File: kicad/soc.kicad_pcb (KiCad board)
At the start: 2 copper layers, 104.1 x 63.5 mm, 18 parts, among them J1 Line Out, J2 PS/2 Keyboard, J3 PS/2 Mouse, J4 Line In, P1 LED MATRIX, P10 CODEC right, P2 ALTERA_DE1_GPIO, P3 Bluetooth, P4 CONN_01X09, P9 CODEC left, U2 DS3234

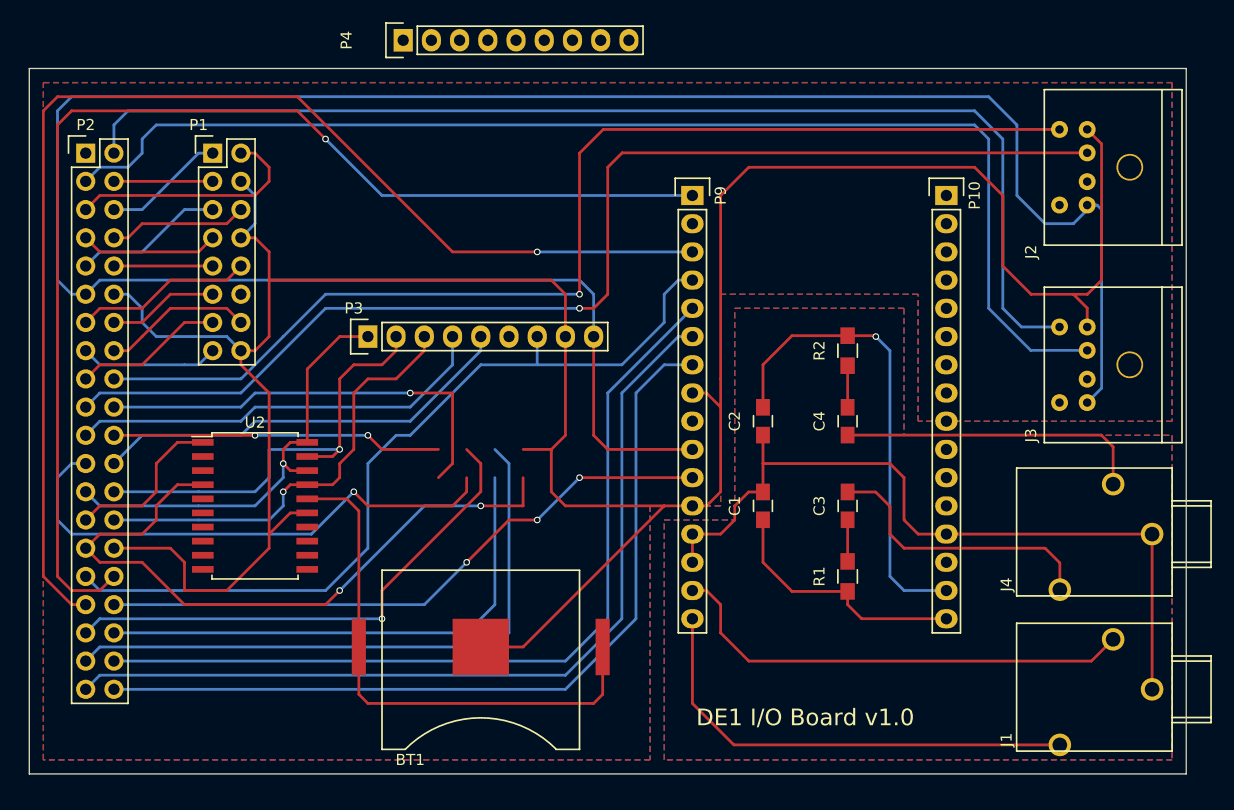
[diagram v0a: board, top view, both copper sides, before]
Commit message: new I/O board to test SSM2603 codec
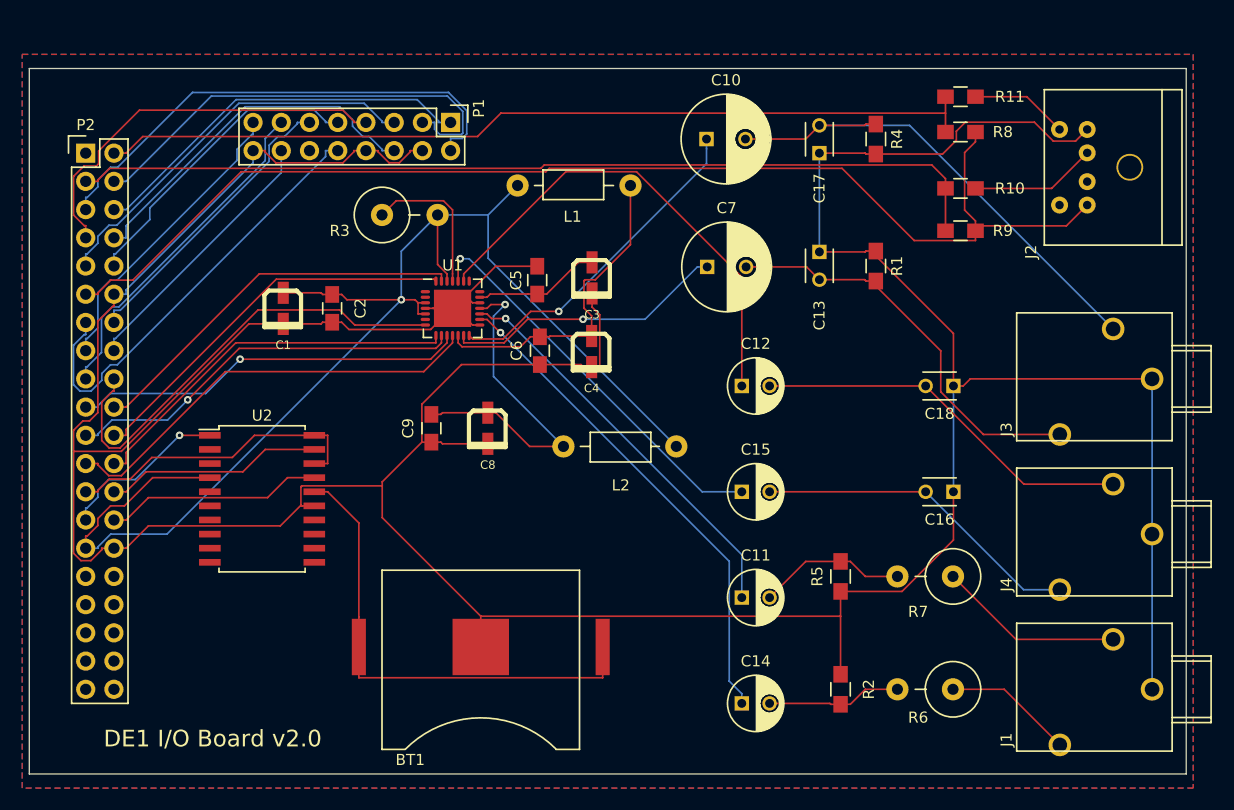
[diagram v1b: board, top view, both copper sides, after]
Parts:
- removed P10: CODEC right, Socket_Strips:Socket_Strip_Straight_1x16
- removed P3: Bluetooth, Socket_Strips:Socket_Strip_Straight_1x09
- removed P4: CONN_01X09, Pin_Headers:Pin_Header_Straight_1x09
- removed P9: CODEC left, Socket_Strips:Socket_Strip_Straight_1x16
- added C10: 220uF, Capacitors_ThroughHole:C_Radial_D8_L11.5_P3.5, F.Cu at (101.6, 67.3)
- added C11: 1uF, Capacitors_ThroughHole:C_Radial_D5_L6_P2.5, F.Cu at (104.8, 108.6)
- added C12: 1uF, Capacitors_ThroughHole:C_Radial_D5_L6_P2.5, F.Cu at (104.8, 89.5)
- added C13: 220pF, Capacitors_ThroughHole:C_Disc_D3_P2.5, F.Cu at (111.8, 77.5)
- added C14: 1uF, Capacitors_ThroughHole:C_Radial_D5_L6_P2.5, F.Cu at (104.8, 118.1)
- added C15: 1uF, Capacitors_ThroughHole:C_Radial_D5_L6_P2.5, F.Cu at (104.8, 99.1)
- added C16: 220pF, Capacitors_ThroughHole:C_Disc_D3_P2.5, F.Cu at (123.8, 99.1)
- added C17: 220pF, Capacitors_ThroughHole:C_Disc_D3_P2.5, F.Cu at (111.8, 68.6)
- added C18: 220pF, Capacitors_ThroughHole:C_Disc_D3_P2.5, F.Cu at (123.8, 89.5)
- added C5: 0.1uF, Capacitors_SMD:C_0805_HandSoldering, F.Cu at (86.4, 80.0)
- added C6: 0.1uF, Capacitors_SMD:C_0805_HandSoldering, F.Cu at (86.6, 86.4)
- added C7: 220uF, Capacitors_ThroughHole:C_Radial_D8_L11.5_P3.5, F.Cu at (101.7, 78.8)
- added C8: 10uF, mstock:UWXCAP-3mm, F.Cu at (81.9, 93.3)
- added C9: 0.1uF, Capacitors_SMD:C_0805_HandSoldering, F.Cu at (76.8, 93.3)
- added L1: FB, Choke_Axial_ThroughHole:Choke_Horizontal_RM10mm, F.Cu at (89.6, 71.5)
- added L2: FB, Choke_Axial_ThroughHole:Choke_Horizontal_RM10mm, F.Cu at (93.9, 95.0)
- added R10: 1k, Resistors_SMD:R_0805_HandSoldering, F.Cu at (124.5, 71.8)
- added R11: 1k, Resistors_SMD:R_0805_HandSoldering, F.Cu at (124.5, 63.5)
- added R3: 100K, Resistors_ThroughHole:Resistor_Vertical_RM5mm, F.Cu at (74.9, 74.1)
- added R4: 47k, Resistors_SMD:R_0805_HandSoldering, F.Cu at (116.8, 67.3)
- added R5: 47k, Resistors_SMD:R_0805_HandSoldering, F.Cu at (113.7, 106.7)
- added R6: 100, Resistors_ThroughHole:Resistor_Vertical_RM5mm, F.Cu at (121.3, 116.8)
- added R7: 100, Resistors_ThroughHole:Resistor_Vertical_RM5mm, F.Cu at (121.3, 106.7)
- added R8: 1k, Resistors_SMD:R_0805_HandSoldering, F.Cu at (124.5, 66.7)
- added R9: 1k, Resistors_SMD:R_0805_HandSoldering, F.Cu at (124.5, 75.6)
- added U1: SSM2603, Housings_DFN_QFN:QFN-28-1EP_5x5mm_Pitch0.5mm, F.Cu at (78.7, 82.5)
- C1: value 10nF -> 10uF; footprint Capacitors_SMD:C_0805_HandSoldering -> mstock:UWXCAP-3mm
- C2: value 10nF -> 0.1uF
- C3, C4: value 1uF -> 10uF; footprint Capacitors_SMD:C_0805_HandSoldering -> mstock:UWXCAP-3mm
- J3: value PS/2 Mouse -> Headphone Out; footprint mstock-pretty:MD-60S -> mstock-pretty:SJI-3513N
- R1, R2: value 470 -> 47k
- moved C1 46.7 mm to (63.5, 82.5), turned to 0 degrees
- moved C2 40.1 mm to (67.9, 82.5), turned to 90 degrees
- moved C3 30.8 mm to (91.3, 79.8), turned to 0 degrees
- moved R2 30.5 mm to (113.7, 116.8), turned to 270 degrees
- moved R1 28.1 mm to (116.8, 78.7)
- moved C4 23.9 mm to (91.3, 86.4), turned to 0 degrees
- moved P1 21.6 mm to (78.6, 65.8), turned to 270 degrees
- moved J3 4.02 mm to (143.5, 88.9)
- moved U2 0.90 mm to (61.6, 99.7)
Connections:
- C1 pad 1: /R_IN -> +3V3
- C1 pad 2: GNDA -> GND
- C2 pad 1: /L_IN -> GND
- C2 pad 2: GNDA -> +3V3
- C3 pad 2: Net-(C3-Pad2) -> GND
- C4 pad 2: Net-(C4-Pad2) -> GND
- J1 pad 1: GNDA -> GND
- J1 pad 2: /L_OUT -> Net-(J1-Pad2)
- J1 pad 3: /R_OUT -> Net-(J1-Pad3)
- J2 pad 1: /Kbd_data -> Net-(J2-Pad1)
- J2 pad 2: (no net) -> Net-(J2-Pad2)
- J2 pad 5: /Kbd_clk -> Net-(J2-Pad5)
- J2 pad 6: (no net) -> Net-(J2-Pad6)
- J3 pad 1: /Mouse_data -> GND
- J3 pad 2: (no net) -> Net-(C10-Pad2)
- J3 pad 3: GND -> Net-(C13-Pad2)
- J4 pad 1: GNDA -> GND
- J4 pad 2: Net-(C4-Pad2) -> Net-(C12-Pad2)
- J4 pad 3: Net-(C3-Pad2) -> Net-(C15-Pad2)
- P1 pad 12: (no net) -> Net-(P1-Pad12)
- P2 pad 18: /Kbd_clk -> /BCLK
- P2 pad 19: /Kbd_data -> /RECDAT
- P2 pad 2: /Mouse_clk -> /Kbd_clk
- P2 pad 20: /IO_17 -> /SDIN
- P2 pad 21: /~BLE_CS -> /PBLRC
- P2 pad 22: /IO_19 -> /SCLK
- P2 pad 23: /IO_20 -> /RECLRC
- P2 pad 24: /BLE_IRQ -> /PBDAT
- P2 pad 3: /Mouse_data -> /Kbd_data
- P2 pad 31: /~RST -> Net-(P2-Pad31)
- P2 pad 32: /~CODEC_XDCS -> Net-(P2-Pad32)
- P2 pad 33: /~CODEC_CS -> Net-(P2-Pad33)
- P2 pad 34: /CODEC_DIRQ -> Net-(P2-Pad34)
- P2 pad 35: /IO_30 -> Net-(P2-Pad35)
- P2 pad 36: /IO_31 -> Net-(P2-Pad36)
- P2 pad 37: /IO_32 -> Net-(P2-Pad37)
- P2 pad 38: /CODEC_SCLK -> Net-(P2-Pad38)
- P2 pad 39: /CODEC_MOSI -> Net-(P2-Pad39)
- P2 pad 40: /CODEC_MISO -> Net-(P2-Pad40)
- R1 pad 1: Net-(C3-Pad1) -> GND
- R1 pad 2: /R_IN -> Net-(C13-Pad2)
- R2 pad 1: Net-(C4-Pad1) -> GND
- R2 pad 2: /L_IN -> Net-(C14-Pad2)
- U2 pad 10: (no net) -> Net-(U2-Pad10)
- U2 pad 11: (no net) -> Net-(U2-Pad11)
- U2 pad 12: (no net) -> Net-(U2-Pad12)
- U2 pad 13: (no net) -> Net-(U2-Pad13)
- U2 pad 14: (no net) -> Net-(U2-Pad14)
- U2 pad 2: (no net) -> Net-(U2-Pad2)
- U2 pad 3: (no net) -> Net-(U2-Pad3)
- U2 pad 5: (no net) -> Net-(U2-Pad5)
- U2 pad 6: (no net) -> Net-(U2-Pad6)
- U2 pad 7: (no net) -> Net-(U2-Pad7)
- U2 pad 8: (no net) -> Net-(U2-Pad8)
- U2 pad 9: (no net) -> Net-(U2-Pad9)
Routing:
- net GND: track 253.6 -> 376.6 mm
- net /~CODEC_CS: track 111.5 -> 0.00 mm, vias 1 -> 0
- net /Mouse_data: track 110.3 -> 0.00 mm
- net /~CODEC_XDCS: track 107.6 -> 0.00 mm, vias 1 -> 0
- net /Mouse_clk: track 105.2 -> 0.00 mm
- net +5V: track 209.2 -> 109.0 mm
- net /CODEC_MOSI: track 79.7 -> 0.00 mm
- net /CODEC_SCLK: track 77.1 -> 0.00 mm
- net /CODEC_MISO: track 76.1 -> 0.00 mm
- net /~RST: track 75.2 -> 0.00 mm
- net GNDA: track 70.2 -> 0.00 mm
- net +3V3: track 61.3 -> 118.8 mm, vias 2 -> 1
- net /CODEC_DIRQ: track 56.8 -> 0.00 mm, vias 3 -> 0
- net /IO_32: track 56.2 -> 0.00 mm
- net /IO_20: track 48.1 -> 0.00 mm, vias 1 -> 0
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- removed copper zone on B.Cu, net GNDA
- removed copper zone on F.Cu, net GNDA
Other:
- net class Default: clearance 0.2 -> 0.1524; trace_width 0.25 -> 0.1524; via_dia 0.6 -> 0.6858; via_drill 0.4 -> 0.3302
- rule trace_clearance: 0.2 -> 0.1524
- rule trace_min: 0.2 -> 0.1524
- rule via_min_drill: 0.3 -> 0.3302
- rule via_min_size: 0.4 -> 0.6604
- board text added: "DE1 I/O Board v2.0"
- board text removed: "DE1 I/O Board v1.0"

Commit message: start of IO board changes
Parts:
- C10, C7: footprint Capacitors_ThroughHole:C_Radial_D8_L11.5_P3.5 -> mstock:UWXCAP-6.3mm
- C11, C12, C14, C15: footprint Capacitors_ThroughHole:C_Radial_D5_L6_P2.5 -> mstock:UWXCAP-3mm
- C13, C16, C17, C18: footprint Capacitors_ThroughHole:C_Disc_D3_P2.5 -> Capacitors_SMD:C_0805_HandSoldering
- R3, R6, R7: footprint Resistors_ThroughHole:Resistor_Vertical_RM5mm -> Resistors_SMD:R_0805_HandSoldering
- moved L2 38.0 mm to (55.9, 96.5), turned to 90 degrees
- moved C16 37.1 mm to (87.0, 103.5), turned to 270 degrees
- moved C18 36.9 mm to (87.0, 91.4), turned to 270 degrees
- moved L1 34.8 mm to (57.8, 85.7)
- moved C13 31.6 mm to (87.0, 97.2)
- moved R1 31.4 mm to (91.4, 97.2)
- moved R7 30.2 mm to (91.4, 111.1), turned to 90 degrees
- moved R6 29.9 mm to (91.4, 118.7), turned to 270 degrees
- moved R4 29.6 mm to (95.9, 88.3)
- moved C17 28.3 mm to (91.4, 88.3)
- moved J3 28.0 mm to (115.6, 87.0)
- moved J4 28.0 mm to (115.6, 101.6)
- moved J1 27.9 mm to (115.6, 116.2)
- moved R5 27.0 mm to (87.0, 111.1)
- moved R2 26.7 mm to (87.0, 118.7)
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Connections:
- J2 pad 1: Net-(J2-Pad1) -> /Kbd_data
- J2 pad 5: Net-(J2-Pad5) -> /Kbd_clk
- P2 pad 31: Net-(P2-Pad31) -> /MCLK
- U1 pad 1: Net-(U1-Pad1) -> /MCLK
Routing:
- net GND: track 376.6 -> 322.7 mm
- net +3V3: track 118.8 -> 75.1 mm
- net /MCLK: track 0.00 -> 43.6 mm, vias 0 -> 1
- net +5V: track 109.0 -> 84.0 mm
- net Net-(C12-Pad1): track 43.2 -> 23.8 mm, vias 0 -> 2
- net /BCLK: track 41.2 -> 22.1 mm
- net Net-(C8-Pad1): track 31.4 -> 50.2 mm
- net Net-(C13-Pad2): track 37.1 -> 54.0 mm
- net /Kbd_clk: track 79.5 -> 64.2 mm
- net Net-(J2-Pad1): track 11.4 -> 0.00 mm
- net /B0: track 41.6 -> 32.5 mm
- net /RECLRC: track 39.1 -> 30.3 mm
- net Net-(J2-Pad5): track 8.79 -> 0.00 mm
- net Net-(R3-Pad1): track 13.6 -> 5.09 mm
- net /Kbd_data: track 83.3 -> 75.0 mm
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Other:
- board size 104.1 x 63.5 mm -> 76.2 x 63.5 mm
- board text added: "DE1 I/O Board v2.1"
- board text removed: "DE1 I/O Board v2.0"

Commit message: more work on new IO board
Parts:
- added D1: PWR, mstock:SM1206POL, F.Cu at (52.1, 120.0)
- added P3: IO, Pin_Headers:Pin_Header_Straight_2x06, F.Cu at (68.6, 137.4)
- added R12: 100K, Resistors_SMD:R_0805_HandSoldering, F.Cu at (55.4, 66.5)
- added R13: 10k, Resistors_SMD:R_0805_HandSoldering, F.Cu at (155.6, 62.1)
- added R14: 10k, Resistors_SMD:R_0805_HandSoldering, F.Cu at (160.7, 62.1)
- added R15: 100, Resistors_SMD:R_0805_HandSoldering, F.Cu at (52.1, 113.3)
- added U3: speakjet, Housings_DIP:DIP-18_W7.62mm, F.Cu at (103.6, 134.9)
- R10, R11: value 1k -> 100K
- moved P1 1.31 mm to (78.7, 64.5)
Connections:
- P2 pad 1: /Serial1 -> /Serial1_TX
- P2 pad 32: Net-(P2-Pad32) -> /speaking
- P2 pad 33: Net-(P2-Pad33) -> /GPIO1
- P2 pad 34: Net-(P2-Pad34) -> /~RESET
- P2 pad 35: Net-(P2-Pad35) -> /GPIO2
- R10 pad 1: Net-(J2-Pad1) -> +3V3
- R10 pad 2: /Kbd_data -> /SCLK
- R11 pad 1: Net-(J2-Pad5) -> +3V3
- R11 pad 2: /Kbd_clk -> /SDIN
- R3 pad 1: Net-(R3-Pad1) -> +3V3
- R3 pad 2: +3V3 -> Net-(R3-Pad2)
- U1 pad 16: Net-(C14-Pad1) -> Net-(R14-Pad2)
- U1 pad 25: Net-(R3-Pad1) -> Net-(R3-Pad2)
- U2 pad 6: Net-(U2-Pad6) -> /~RESET
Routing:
- net GND: track 322.7 -> 0.00 mm
- net +5V: track 84.0 -> 0.00 mm
- net +3V3: track 75.1 -> 0.00 mm, vias 1 -> 0
- net /Kbd_data: track 75.0 -> 0.00 mm
- net /Kbd_clk: track 64.2 -> 0.00 mm
- net Net-(C13-Pad2): track 54.0 -> 0.00 mm
- net Net-(C8-Pad1): track 50.2 -> 0.00 mm, vias 1 -> 0
- net Net-(BT1-Pad1): track 46.2 -> 0.00 mm
- net Net-(C10-Pad2): track 45.5 -> 0.00 mm
- net /MCLK: track 43.6 -> 0.00 mm, vias 1 -> 0
- net Net-(C14-Pad1): track 42.2 -> 0.00 mm, vias 2 -> 0
- net /G0: track 39.6 -> 0.00 mm
- net /B: track 36.1 -> 0.00 mm
- net /CLK: track 36.0 -> 0.00 mm
- net /R1: track 35.9 -> 0.00 mm
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- removed copper zone on B.Cu, net GND
- removed copper zone on F.Cu, net GND
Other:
- board text added: "DE1 I/O Board v2.2"
- board text removed: "DE1 I/O Board v2.1"

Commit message: additions to the support board
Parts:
- added C19: 0.1uF, Capacitors_SMD:C_0805_HandSoldering, F.Cu at (140.0, 66.0)
- added C20: 0.1uF, Capacitors_SMD:C_0805_HandSoldering, F.Cu at (150.9, 77.0)
- added C21: 0.1uF, Capacitors_SMD:C_0805_HandSoldering, F.Cu at (151.1, 63.8)
- added C22: 0.1uF, Capacitors_SMD:C_0805_HandSoldering, F.Cu at (131.8, 70.1)
- added C23: 0.1uF, Capacitors_SMD:C_0805_HandSoldering, F.Cu at (147.6, 87.6)
- added D2: TX1, mstock:SM1206POL, F.Cu at (125.0, 91.7)
- added D3: TX0, mstock:SM1206POL, F.Cu at (128.3, 105.2)
- added D4: RX0, mstock:SM1206POL, F.Cu at (127.3, 77.7)
- added J5: Headphone, mstock-pretty:SJ-4351X-SMT, F.Cu at (133.1, 123.2)
- added R16: 330, Resistors_SMD:R_0805_HandSoldering, F.Cu at (148.8, 98.8)
- added R17: 330, Resistors_SMD:R_0805_HandSoldering, F.Cu at (127.8, 85.6)
- added R18: 330, Resistors_SMD:R_0805_HandSoldering, F.Cu at (128.5, 63.2)
- added U4: MAX3232, mstock-pretty:SOIC-16, F.Cu at (85.1, 141.0)
- J3: value Headphone Out -> DB9; footprint mstock-pretty:SJI-3513N -> mstock-pretty:DB9F
- R15: value 100 -> 330
- moved J3 50.1 mm to (147.1, 126.0)
- moved R13 40.4 mm to (134.1, 96.3)
- moved R14 27.5 mm to (138.2, 77.7)
- moved BT1 2.47 mm to (66.8, 115.1)
- moved J2 1.05 mm to (112.8, 68.8)
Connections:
- J3 pad 1: GND -> Net-(J3-Pad1)
- J3 pad 2: Net-(C10-Pad2) -> Net-(J3-Pad2)
- J3 pad 3: Net-(C13-Pad2) -> Net-(J3-Pad3)
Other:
- board text added: "DE1 I/O Board v2.5"
- board text removed: "DE1 I/O Board v2.2"
